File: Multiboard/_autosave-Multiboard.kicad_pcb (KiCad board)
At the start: 2 copper layers, 150 x 120 mm, 192 parts, among them J1 Conn_01x20_Socket, J2 Conn_01x20_Socket, J3 Debug, J4 USB_C_Receptacle_USB2.0_16P, J5 Conn_01x06_Socket, J6 Conn_02x20_Odd_Even, J7 Conn_02x20_Odd_Even, J8 USB_C_Receptacle_USB2.0_16P, Q1 Q_Dual_NMOS_G1S2G2D2S1D1, Q2 Q_Dual_NMOS_G1S2G2D2S1D1, Q3 Q_Dual_NMOS_G1S2G2D2S1D1, Q4 Q_Dual_NMOS_G1S2G2D2S1D1, Q5 Q_Dual_NMOS_G1S2G2D2S1D1, Q6 Q_Dual_NMOS_G1S2G2D2S1D1, Q7 Q_Dual_NMOS_G1S2G2D2S1D1, SW1 BOOT0, SW2 NRST, SW3 SW_SPST, SW4 SW_SPST, SW5 SW_SPST, SW6 SW_SPST, SW7 KEY, SW8 SW_SPST, U1 STM32F411RET6, U2 MAX662AESA_T, U3 MCP1792x-3302xCB, U4 FT2232HL-REEL, U5 93LCxxC, U6 LCMXO2-1200ZE-1TG144C, U7 FAN1112, U8 NCP1117, Y1 32.768KHz, Y2 25MHz, Y3 12MHz

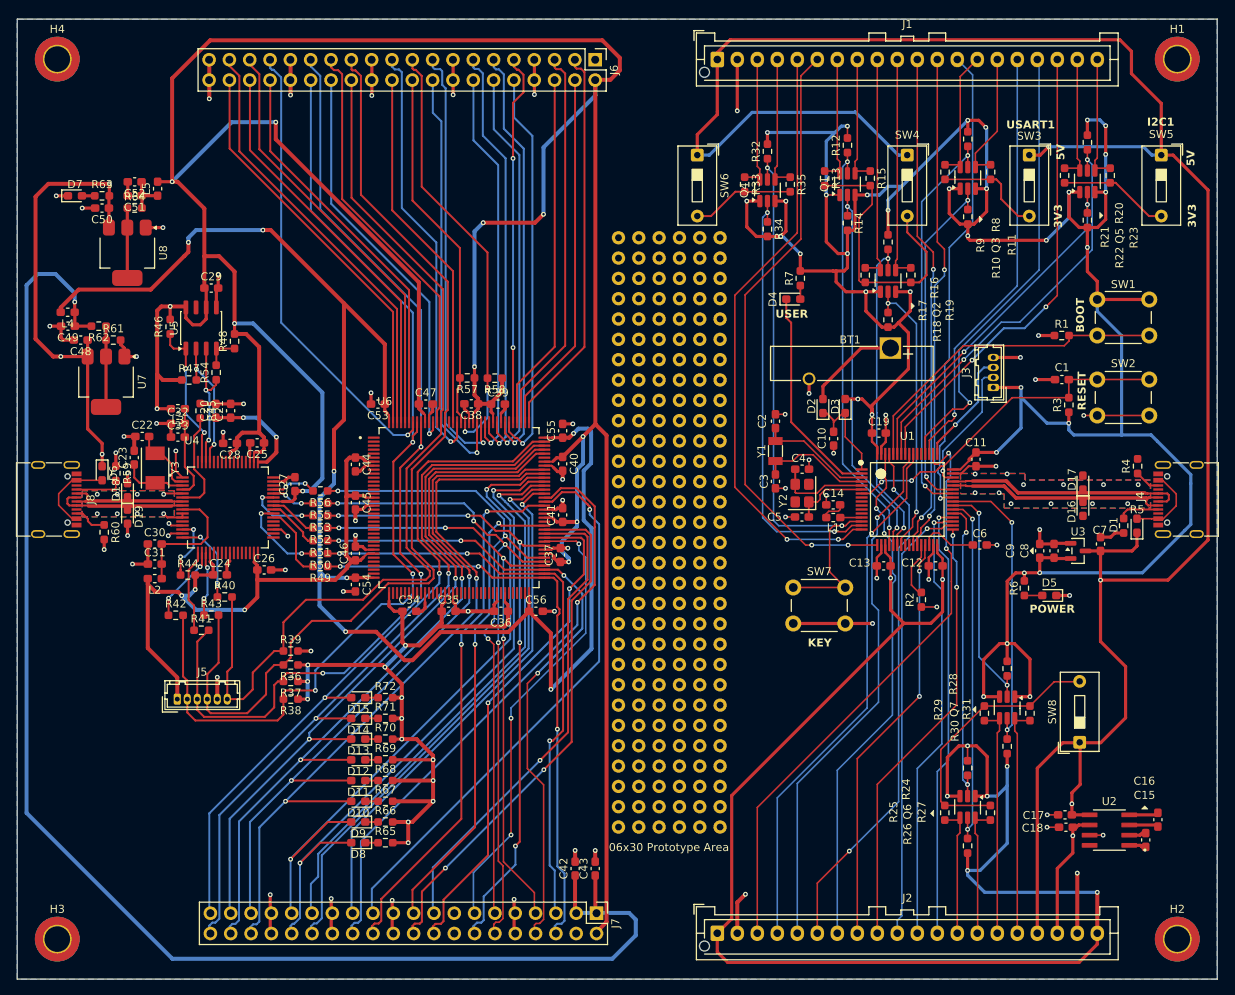
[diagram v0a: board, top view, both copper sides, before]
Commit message: added silkscreen layer
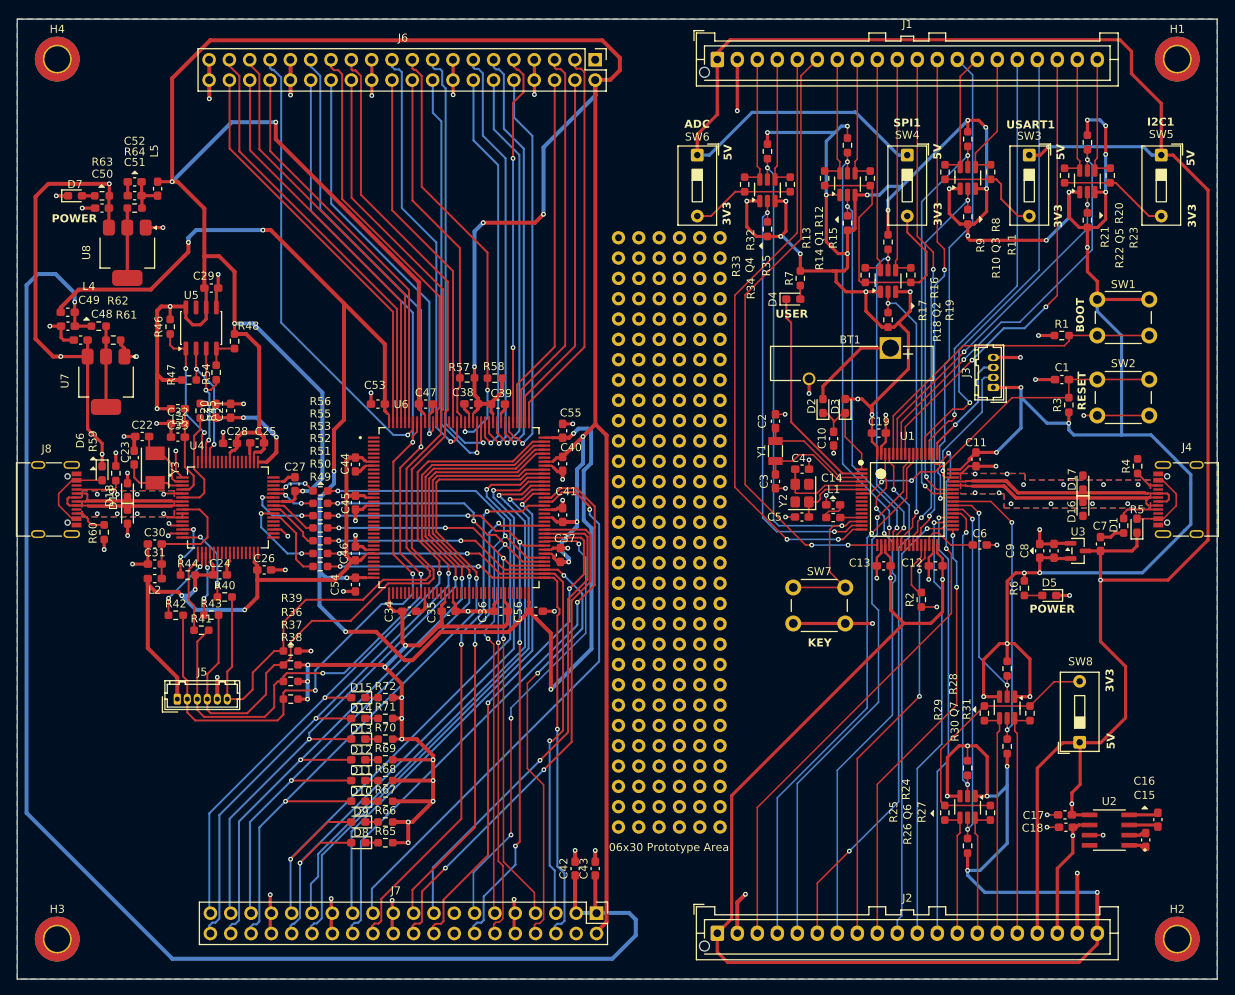
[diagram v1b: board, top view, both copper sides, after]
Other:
- board text added: "ADC"
- board text added: "SPI1"
